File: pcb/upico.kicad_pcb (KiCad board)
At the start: 6 copper layers, 33.5 x 77 mm, 74 parts, among them J1 uConsoleEXT, J2 uPico Connect, J3 USB_C, J4 Camera, J5 uConsoleSpeaker, J6 uConsoleSpeaker, U1 W25Q32JV, U2 RP2040, U3 USBLC6-2P6, U4 USBLC6-2P6, U5 AP22652_3x, U6 AP22652_3x, U7 AP22652_3x, Y1 12MHz

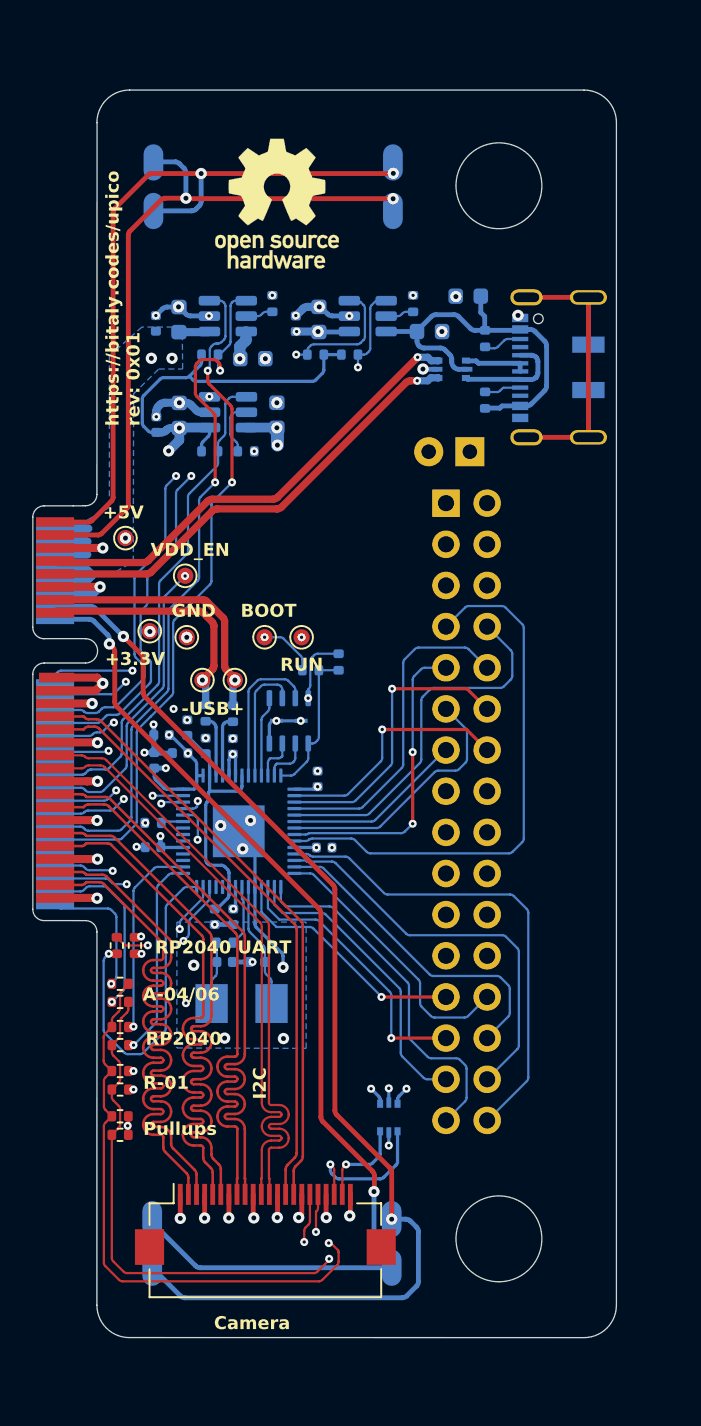
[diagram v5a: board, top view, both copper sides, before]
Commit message: add BOM
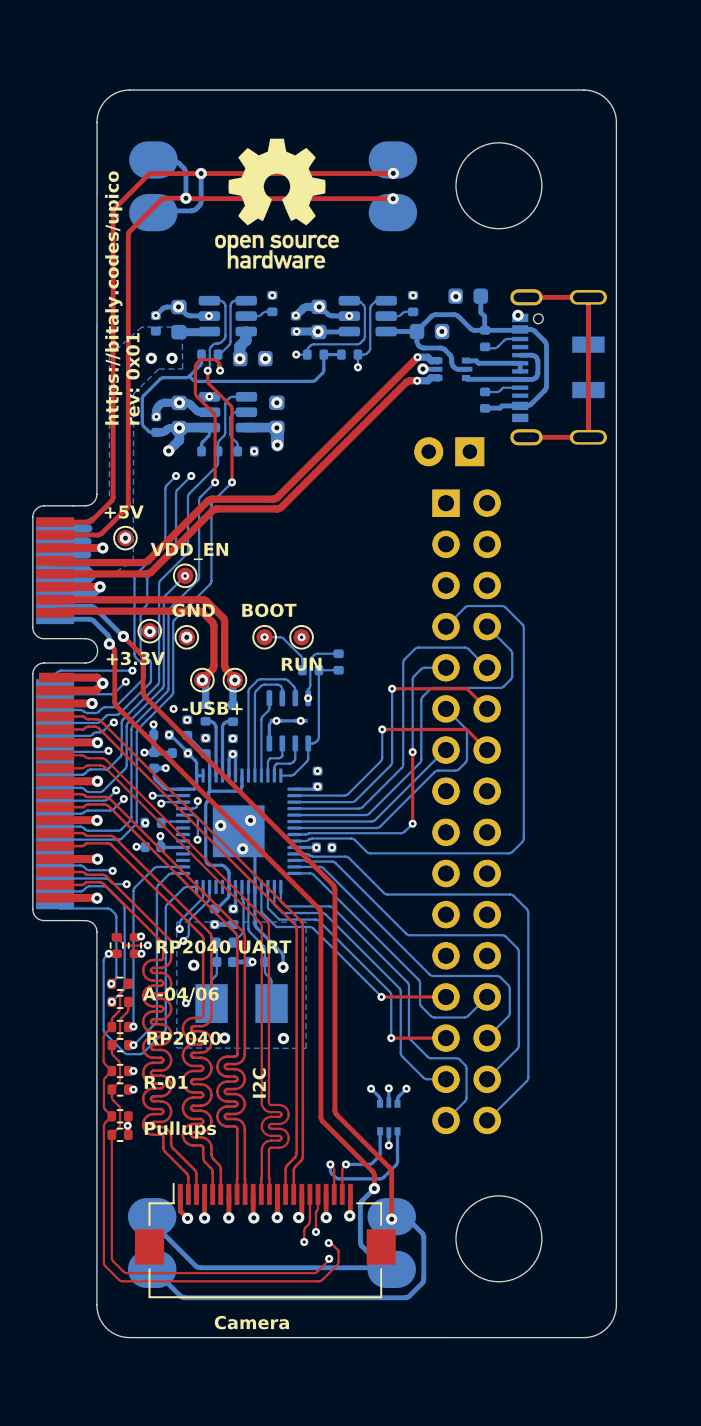
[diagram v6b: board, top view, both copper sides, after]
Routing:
- net /SPK_RN: track 66.0 -> 67.0 mm

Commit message: control app refactoring
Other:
- board text added: "A04/A06"
- board text added: "R01/CM3"
- board text removed: "A-04/06"
- board text removed: "R-01"
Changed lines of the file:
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@@
     (effects (font (size 0.8 0.8) (thickness 0.15) bold) (justify left bottom))
   )
-  (gr_text "A-04/06   " (at 62.7888 112.961799) (layer "F.SilkS" knockout)
+  (gr_text "A04/A06   " (at 62.7888 112.961799) (layer "F.SilkS" knockout)
     (effects (font (size 0.8 0.8) (thickness 0.15) bold) (justify left bottom))
   )
-  (gr_text "R-01    " (at 62.8142 118.4148) (layer "F.SilkS" knockout)
+  (gr_text "R01/CM3" (at 62.8142 118.4148) (layer "F.SilkS" knockout)
     (effects (font (size 0.8 0.8) (thickness 0.15) bold) (justify left bottom))
   )

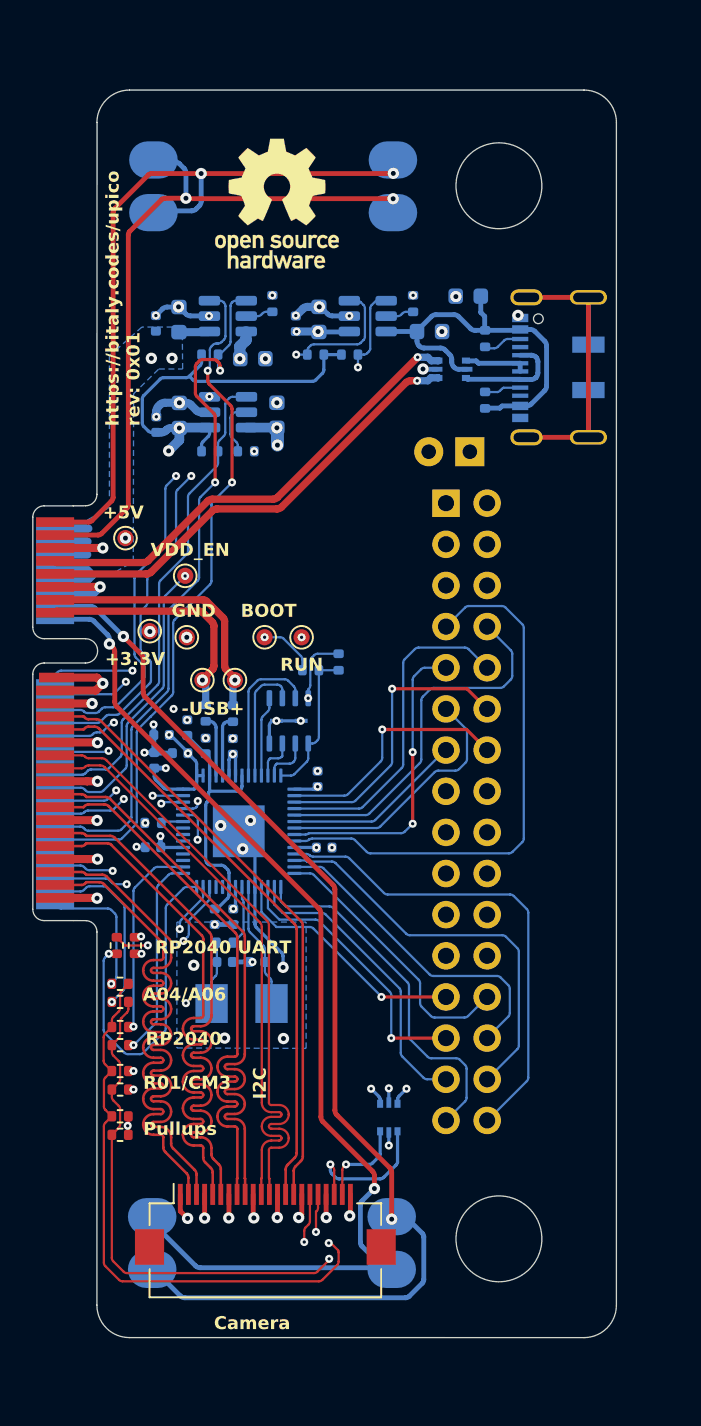
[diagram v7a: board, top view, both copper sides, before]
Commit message: change USB connector
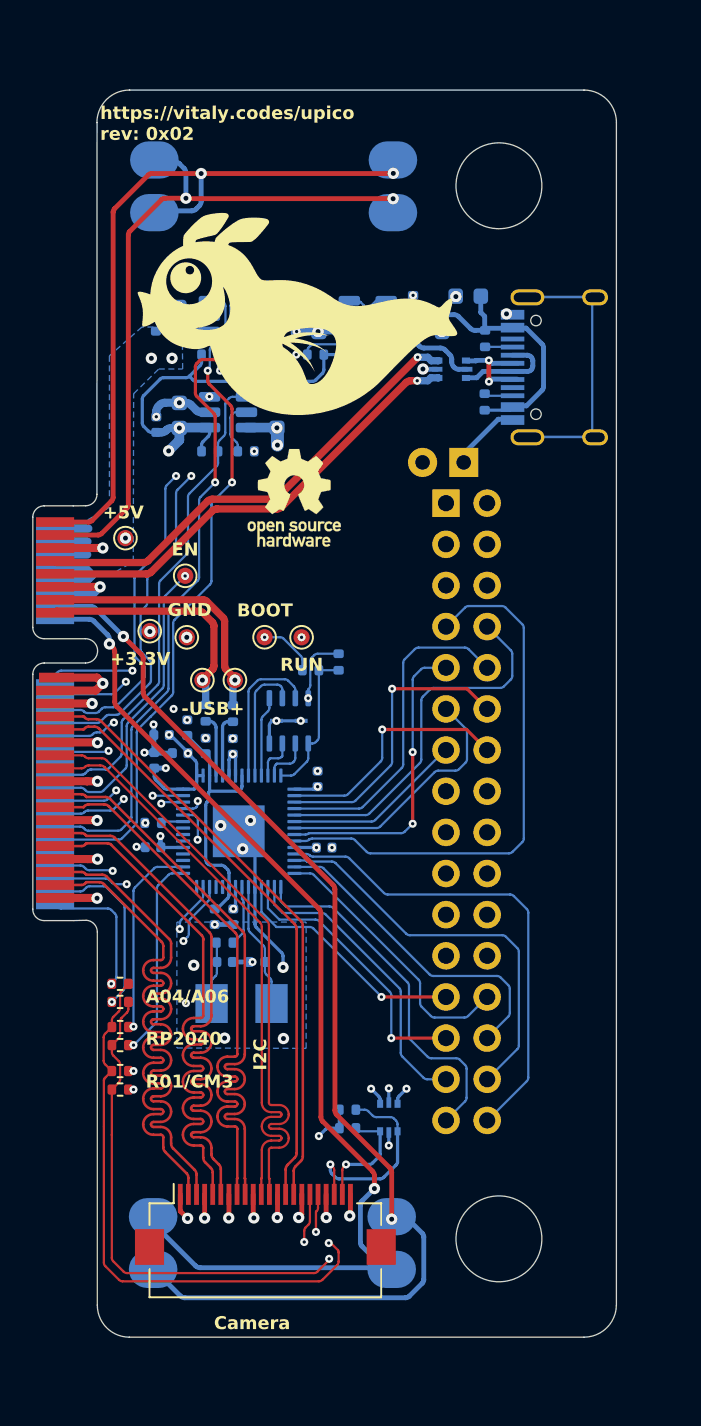
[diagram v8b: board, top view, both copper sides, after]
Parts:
- removed the R13 at (62.3, 109.5)
- removed the R14 at (61.2, 109.5)
- removed the REF** at (71.1, 63.7)
- added REF**: OSHW-Logo_5.7x6mm_SilkScreen, Symbol:OSHW-Logo_5.7x6mm_SilkScreen, F.Cu at (72.1, 81.8)
- J3: value USB_C -> USB_C_Receptacle_USB2.0; footprint @jb:USB_C_Receptacle_JAE_DX07S016JA3R1500 -> Connector_USB:USB_C_Receptacle_HRO_TYPE-C-31-M-12
- R10, R11: moved to B.Cu
- moved R11 14.1 mm to (75.4, 120.8), turned to 0 degrees
- moved R10 14.0 mm to (75.4, 119.6), turned to 0 degrees
- moved J3 2.46 mm to (89.7, 73.8)
- moved D1 0.76 mm to (82.6, 79.7)
- moved R15 0.11 mm to (83.9, 75.9)
- renumbered R15 to R12, R16 to R13, R12 to R14, R17 to R15, R18 to R16, R19 to R17, R20 to R18, R21 to R19, R22 to R20, R23 to R21, R24 to R22, R25 to R23
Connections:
- J1 pad 26: /UART_TX -> unconnected-(J1-GPIO32-Pad26)
- J1 pad 28: /UART_RX -> unconnected-(J1-GPIO33-Pad28)
- J3 pad A12: (no net) -> GND
- U2 pad 27: Net-(U2-GPIO16) -> unconnected-(U2-GPIO16-Pad27)
- U2 pad 28: Net-(U2-GPIO17) -> unconnected-(U2-GPIO17-Pad28)
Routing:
- net /UART_TX: track 21.2 -> 0.00 mm, vias 2 -> 0
- net Net-(U2-GPIO17): track 20.4 -> 0.00 mm, vias 1 -> 0
- net /UART_RX: track 17.3 -> 0.00 mm, vias 2 -> 0
- net Net-(U2-GPIO16): track 8.46 -> 0.00 mm, vias 2 -> 0
- net +3.3V: track 97.9 -> 102.7 mm
- net GND: track 66.8 -> 71.5 mm
- net unconnected-(J1-GPIO32-Pad26): track 0.00 -> 3.92 mm, vias 0 -> 1
- net unconnected-(J1-GPIO33-Pad28): track 0.00 -> 3.39 mm, vias 0 -> 1
- net unconnected-(U2-GPIO16-Pad27): track 0.00 -> 3.17 mm, vias 0 -> 1
- net /I2C_SCL: track 49.8 -> 52.8 mm
- net unconnected-(J3-SHIELD-PadS1): track 22.1 -> 25.1 mm
- net Net-(J3-D+-PadA6): track 3.92 -> 6.43 mm, vias 0 -> 2
- net /I2C_SDA: track 43.1 -> 44.3 mm
- net Net-(D1-A): track 33.8 -> 33.2 mm
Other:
- outline, holes or cut-outs redrawn
- board text added: "EN"
- board text added: "https://vitaly.codes/upico rev: 0x02"
- board text removed: "Pullups"
- board text removed: "RP2040 UART"
- board text removed: "VDD_EN"
- board text removed: "https://bitaly.codes/upico rev: 0x01"
